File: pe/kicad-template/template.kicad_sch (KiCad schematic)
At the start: 9 parts, among them IC1 TS30013-M050QFNR, J1 Conn_01x02, J2 PK_HOLD_OUT, U1 MCP6004

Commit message: added other components and some wiring
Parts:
- removed C2: C0603C104M3VACTU, capacitor:CAPC1608X90N, symbol capacitor:C0603C104M3VACTU
- added C2: TMK107BBJ106MA-T, TMK107BBJ106MA-T:CAPC1709X100N, symbol outside_symbols:TMK107BBJ106MA-T
- added L1: ASPIAIG-S6055-100M-T, ASPIAIG-S6055-100M-T:IND_ASPIAIG-S6055-100M-T, symbol outside_symbols:ASPIAIG-S6055-100M-T
- added L2: L_Small, symbol KiCad:L_Small
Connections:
- net GND: now also IC1.14 (PGND_1)
- net at IC1.1 (VSW_1): now also L2.2
- net at IC1.2 (VCC_1): now also L1.2
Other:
- moved on the sheet: C1, D1, IC1, J1, J2, R1, R2, U1A, U1B

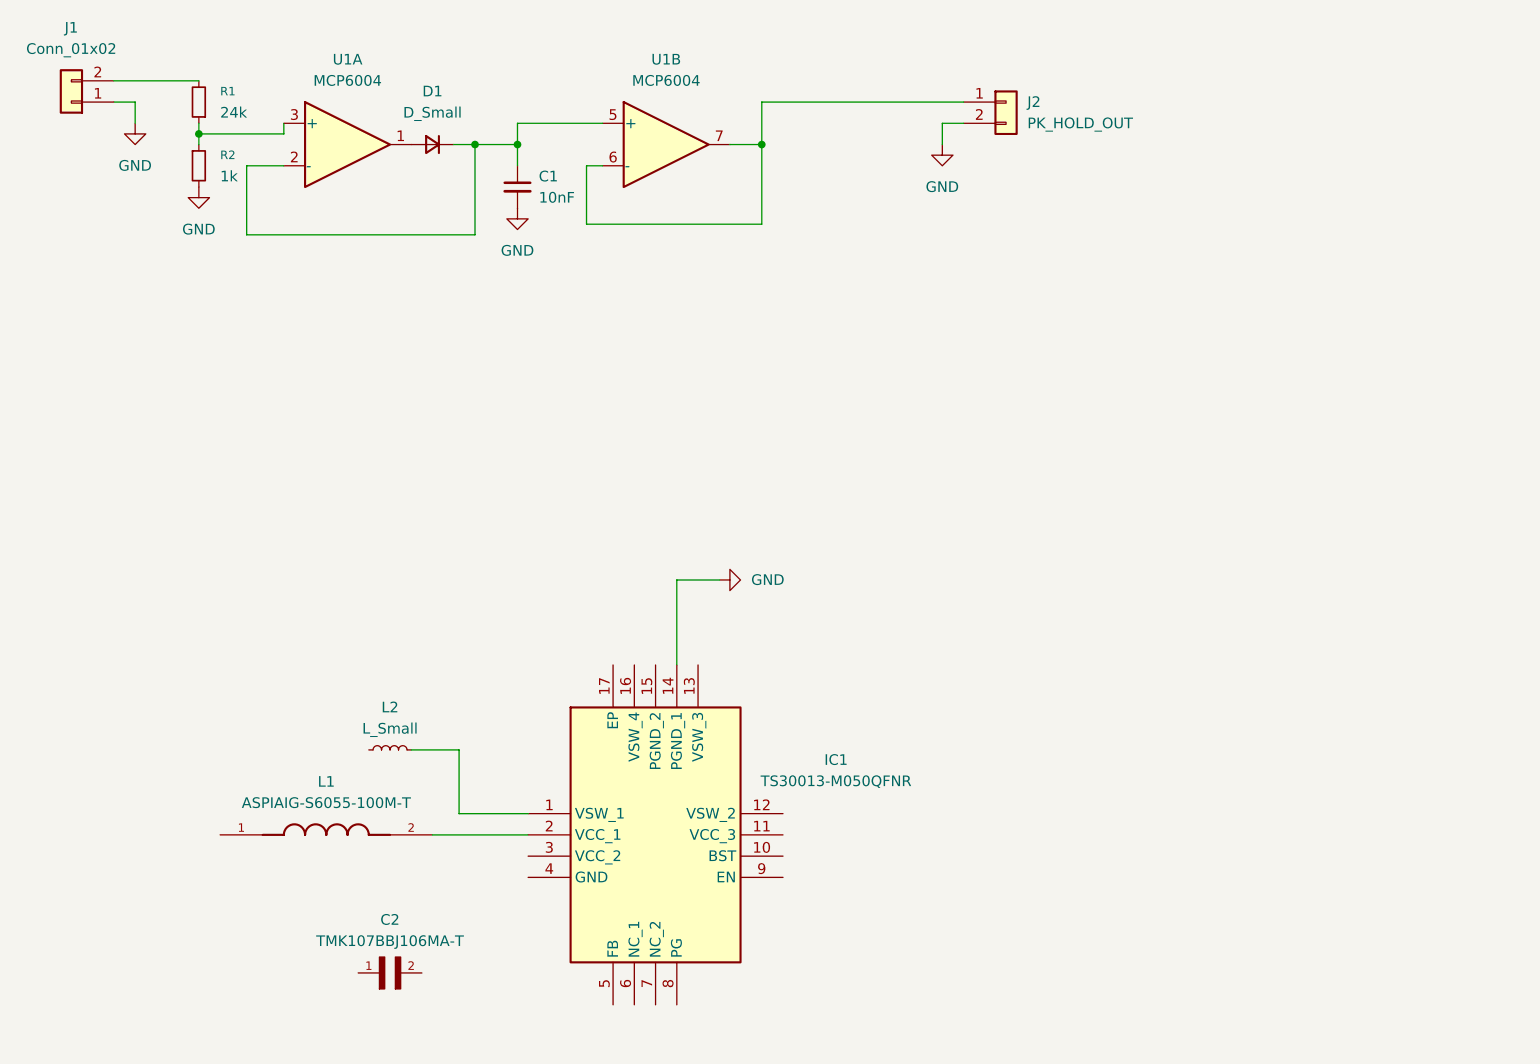
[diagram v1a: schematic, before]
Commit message: Added some more components to schematic and a placeholder for inductor
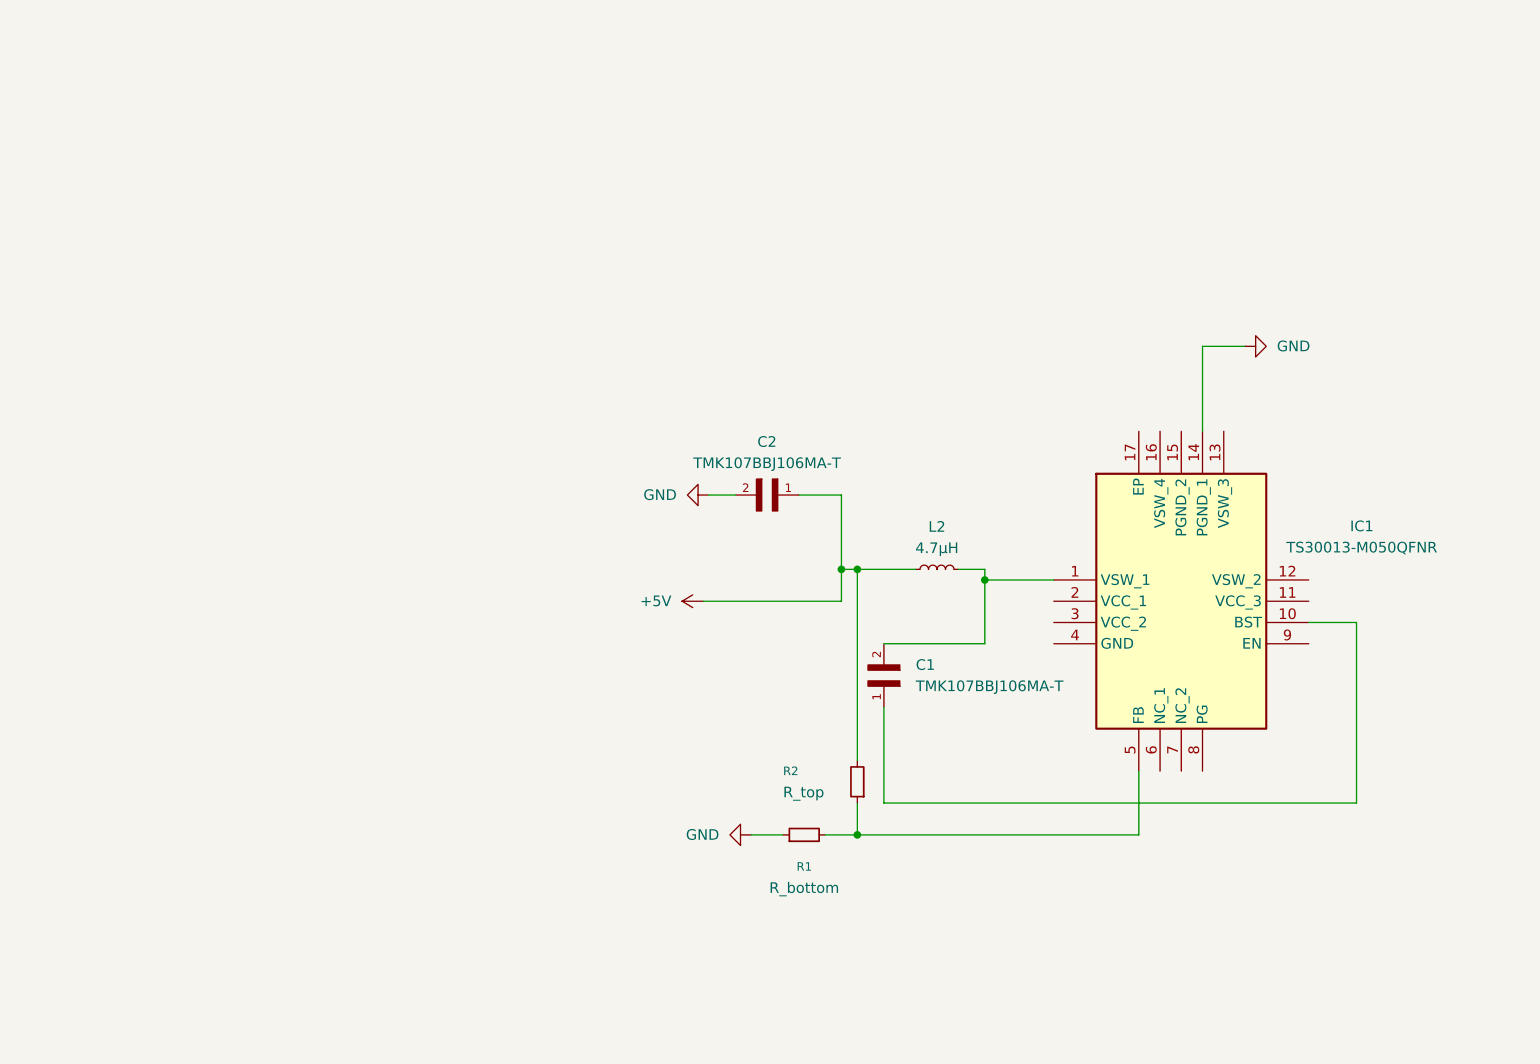
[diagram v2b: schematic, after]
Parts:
- removed C1: 10nF, Capacitor_SMD:CP_Elec_6.3x3, symbol KiCad:C_Small
- removed D1: D_Small, Diode_SMD:D_0201_0603Metric, symbol KiCad:D_Small
- removed J1: Conn_01x02, Connector_PinSocket_2.54mm:PinSocket_1x06_P2.54mm_Vertical, symbol KiCad:Conn_01x02
- removed J2: PK_HOLD_OUT, Connector_PinSocket_2.54mm:PinSocket_1x06_P2.54mm_Vertical, symbol KiCad:Conn_01x02
- removed L1: ASPIAIG-S6055-100M-T, ASPIAIG-S6055-100M-T:IND_ASPIAIG-S6055-100M-T, symbol outside_symbols:ASPIAIG-S6055-100M-T
- removed U1: MCP6004, formula_slug_footprint_library:SOIC-8_ISO1044BD, symbol KiCad:MCP6004
- added C2: TMK107BBJ106MA-T, TMK107BBJ106MA-T:CAPC1709X100N, symbol outside_symbols:TMK107BBJ106MA-T
- L2: value L_Small -> 4.7µH
- R1: value 24k -> R_bottom; footprint Resistor_SMD:R_0603_1608Metric -> (none)
- R2: value 1k -> R_top; footprint Resistor_SMD:R_0603_1608Metric -> (none)
- renumbered C2 to C1
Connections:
- net GND: now also R1.1, C2.2; no longer R2.2
- net at R2.1: now also IC1.5 (FB), R1.2; no longer R1.1
- net +5V: now reaches L2.1
- net +5V: now also R2.2, C2.1
- net at IC1.1 (VSW_1), L2.2: now also C1.2
- net at C1.1: now also IC1.10 (BST)
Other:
- moved on the sheet: C1, IC1, L2

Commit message: schematic basically done by my understanding, also attached pdf of activity 2 from docs to show some reasoning hopefully
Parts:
- removed L2: 4.7µH, symbol KiCad:L_Small
- added C3: 10µF, outside_footprints:CAPC1709X100N, symbol outside_symbols:TMK107BBJ106MA-T
- added L1: 10µH, outside_footprints:IND_ASPIAIG-S6055-100M-T, symbol outside_symbols:ASPIAIG-S6055-100M-T
- C1, C2: value TMK107BBJ106MA-T -> 10µF; footprint TMK107BBJ106MA-T:CAPC1709X100N -> outside_footprints:CAPC1709X100N
- IC1: footprint QFN50P300X300X100-17N-D -> outside_footprints:QFN50P300X300X100-17N-D
- R1, R2: footprint (none) -> Resistor_SMD:R_0603_1608Metric
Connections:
- net +5V: now also L1.1
- net GND: now also IC1.4 (GND), C3.2
- net at C1.2, IC1.1 (VSW_1): now also L1.2
- net at IC1.11 (VCC_3): now also IC1.12 (VSW_2), IC1.9 (EN)
- net at IC1.13 (VSW_3): now also IC1.15 (PGND_2), IC1.16 (VSW_4), IC1.17 (EP)
- net +12V: now reaches IC1.2 (VCC_1)
- net +12V: now also C3.1
- net at IC1.6 (NC_1): now also IC1.7 (NC_2), IC1.8 (PG)
